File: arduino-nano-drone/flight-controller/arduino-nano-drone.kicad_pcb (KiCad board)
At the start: 2 copper layers, 62.2 x 70.3 mm, 12 parts

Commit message: Reviewed schematics and boards
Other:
- board text added: "Jeśli zrobisz lustrzane obicie komponentów (arduino po prawej), to będziesz mieć dużo lepiej poprowadzone ścieżki"
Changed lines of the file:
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@@
+    (effects (font (size 1 1) (thickness 0.15)) (justify left bottom))
+  )
+  (gr_text "Jeśli zrobisz lustrzane obicie komponentów (arduino po prawej), to będziesz mieć dużo lepiej poprowadzone ścieżki" (at 119.425 63.5) (layer "User.8")
     (effects (font (size 1 1) (thickness 0.15)) (justify left bottom))
   )

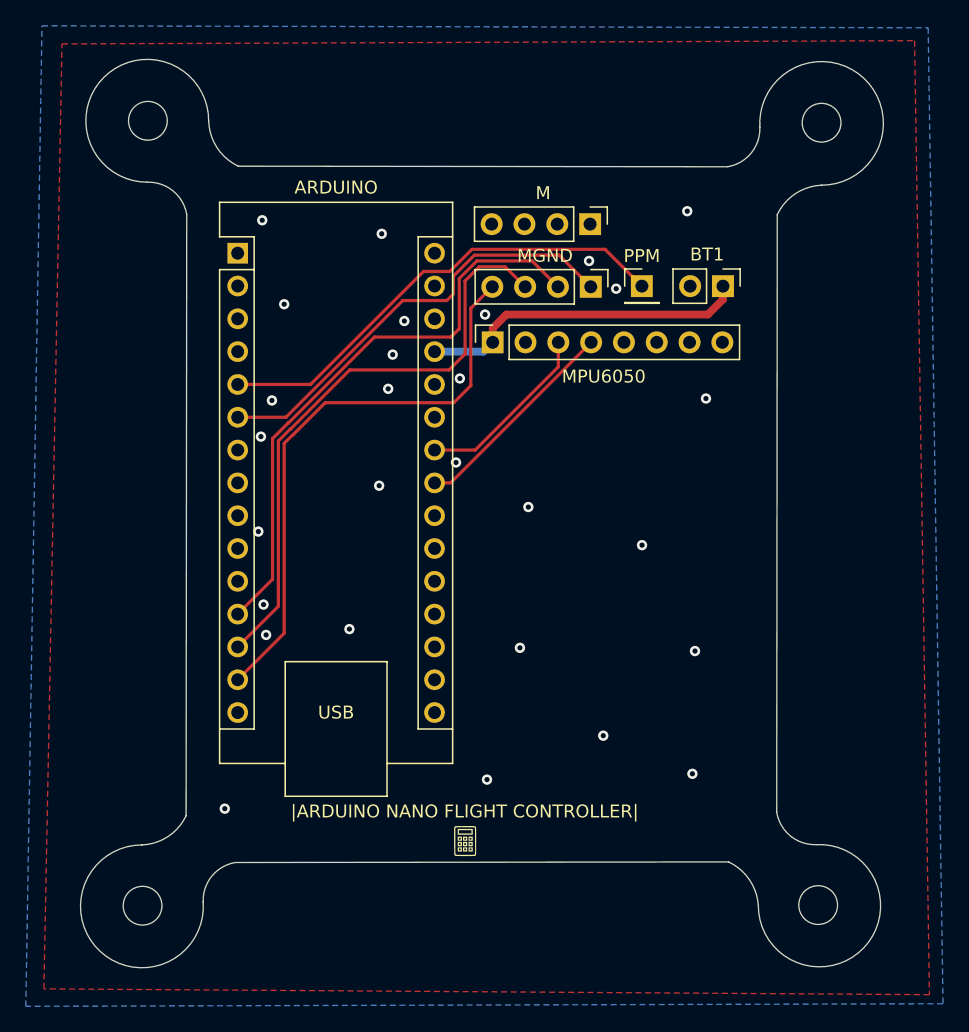
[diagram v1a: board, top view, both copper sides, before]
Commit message: project 8 / arduino nano drone / improved schematics and pcb layout
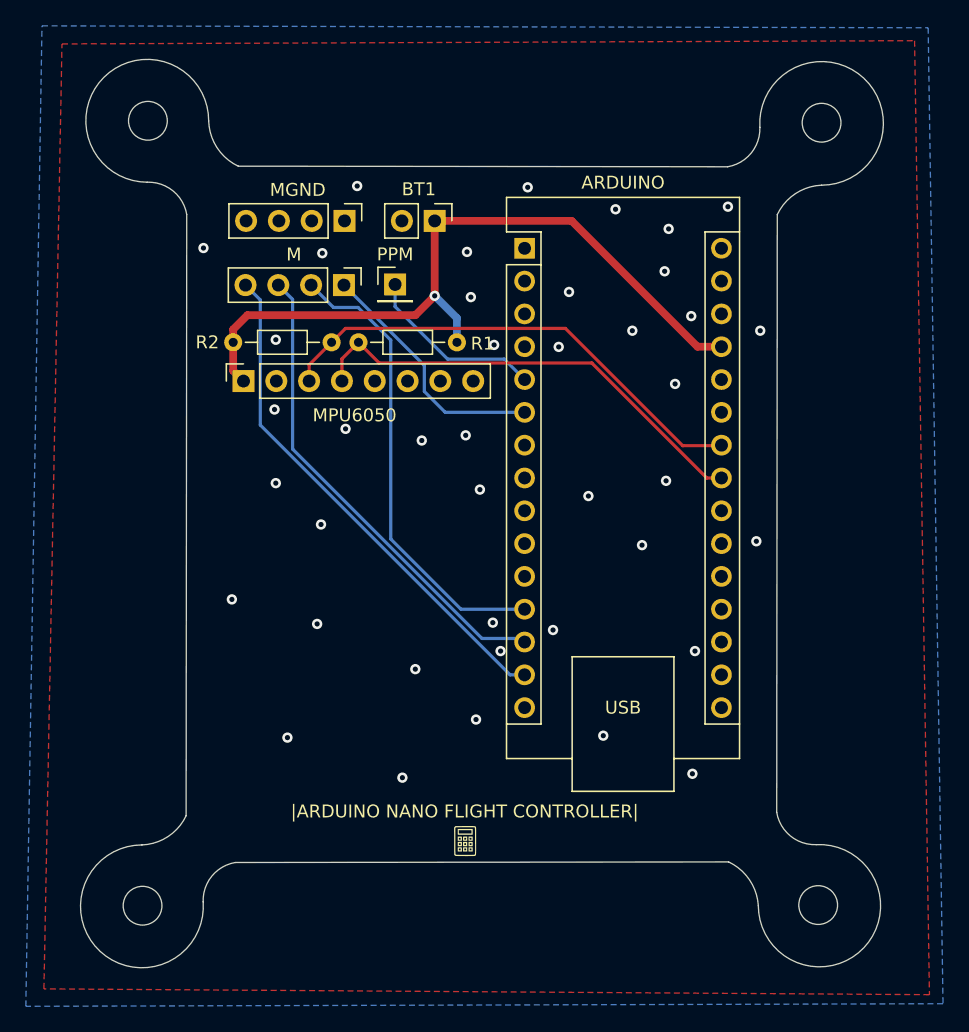
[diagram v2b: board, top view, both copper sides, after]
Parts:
- added R1: 4.7k, Resistor_THT:R_Axial_DIN0204_L3.6mm_D1.6mm_P7.62mm_Horizontal, F.Cu at (115.2, 51.8)
- added R2: 4.7k, Resistor_THT:R_Axial_DIN0204_L3.6mm_D1.6mm_P7.62mm_Horizontal, F.Cu at (97.9, 51.8)
- M: renamed from MGND; value motor pins -> Conn_01x04_Pin
- PPM: value ppm_pin -> Conn_01x01_Pin
- moved BT1 22.9 mm to (113.5, 42.4)
- moved ARDUINO 22.2 mm to (120.5, 44.5)
- moved MPU6050 19.5 mm to (98.7, 54.8)
- moved M 19.1 mm to (106.5, 47.4)
- moved PPM 19.1 mm to (110.4, 47.3)
- moved MGND 19.0 mm to (106.5, 42.4)
- renumbered M to MGND
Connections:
- net /A4 renamed /SDA
- net /A5 renamed /SCL
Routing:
- net VCC: track 25.7 -> 57.4 mm, vias 0 -> 1
- net /SCL: track 14.1 -> 38.1 mm
- net Net-(A2-D2): track 36.8 -> 14.1 mm
- net /SDA: track 16.6 -> 36.0 mm
- net Net-(A2-D3): track 34.3 -> 19.2 mm
- net Net-(A2-D9): track 45.6 -> 35.9 mm
- net Net-(A2-D10): track 45.9 -> 37.4 mm
- net Net-(A2-D11): track 44.4 -> 39.8 mm
- net GND: vias 28 -> 41
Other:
- board text removed: "Jeśli zrobisz lustrzane obicie komponentów (arduino po prawej), to będziesz mieć dużo lepiej poprowadzone ścieżki"
